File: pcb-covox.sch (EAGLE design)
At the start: 25 parts, among them X2 MJ-2135MJ-2135

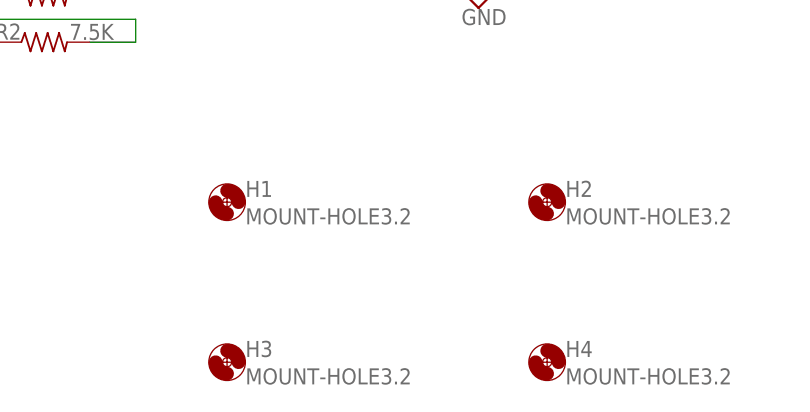
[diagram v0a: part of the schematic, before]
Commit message: corrected bug in size of audio connector
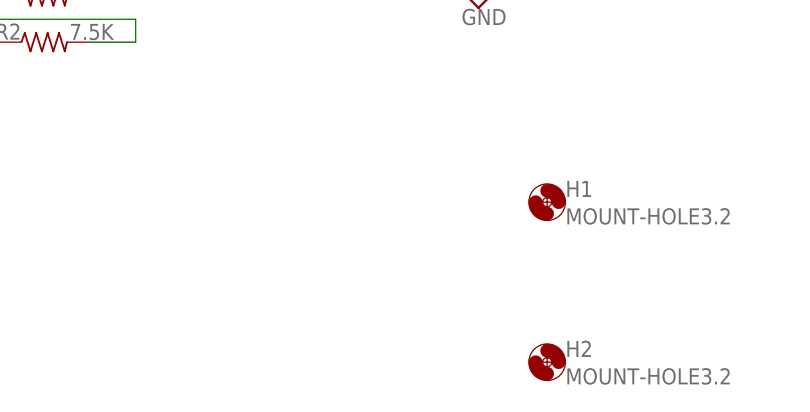
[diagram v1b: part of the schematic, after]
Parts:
- removed H3, H4: MOUNT-HOLE3.2, holes:MOUNT-HOLE3.2
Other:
- moved on the sheet: H1, H2
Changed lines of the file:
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@@
 <part name="H1" library="holes" deviceset="MOUNT-HOLE" device="3.2"/>
 <part name="H2" library="holes" deviceset="MOUNT-HOLE" device="3.2"/>
-<part name="H3" library="holes" deviceset="MOUNT-HOLE" device="3.2"/>
-<part name="H4" library="holes" deviceset="MOUNT-HOLE" device="3.2"/>
 </parts>
 <sheets>
@@
 <instance part="SUPPLY1" gate="GND" x="129.54" y="20.32"/>
 <instance part="X2" gate="G$1" x="167.64" y="38.1" rot="MR0"/>
-<instance part="H1" gate="G$1" x="101.6" y="-2.54"/>
-<instance part="H2" gate="G$1" x="137.16" y="-2.54"/>
-<instance part="H3" gate="G$1" x="101.6" y="-20.32"/>
-<instance part="H4" gate="G$1" x="137.16" y="-20.32"/>
+<instance part="H1" gate="G$1" x="137.16" y="-2.54"/>
+<instance part="H2" gate="G$1" x="137.16" y="-20.32"/>
 </instances>
 <busses>
